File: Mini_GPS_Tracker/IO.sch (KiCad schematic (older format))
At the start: 10 parts, among them J1 Conn_ARM_JTAG_SWD_10, J4 Qwiic_Connector, SW1 SW_Push

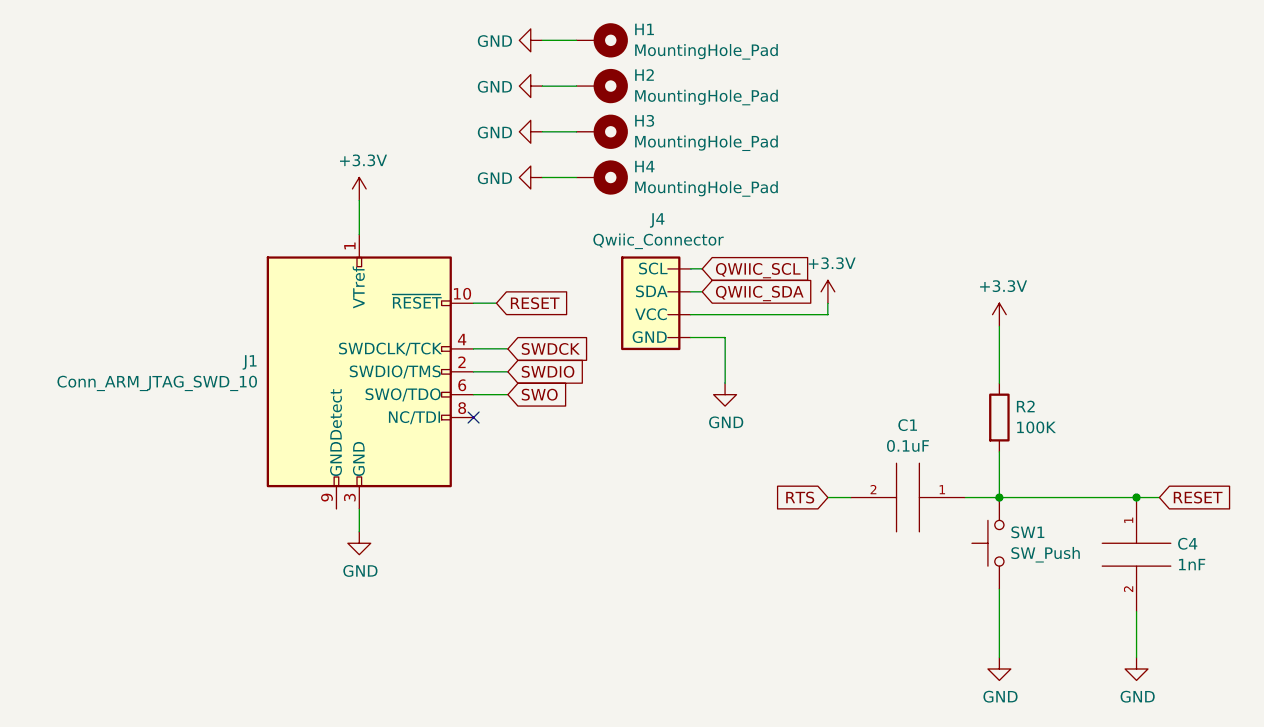
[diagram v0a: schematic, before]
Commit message: Add files via upload
Breaking out more pins
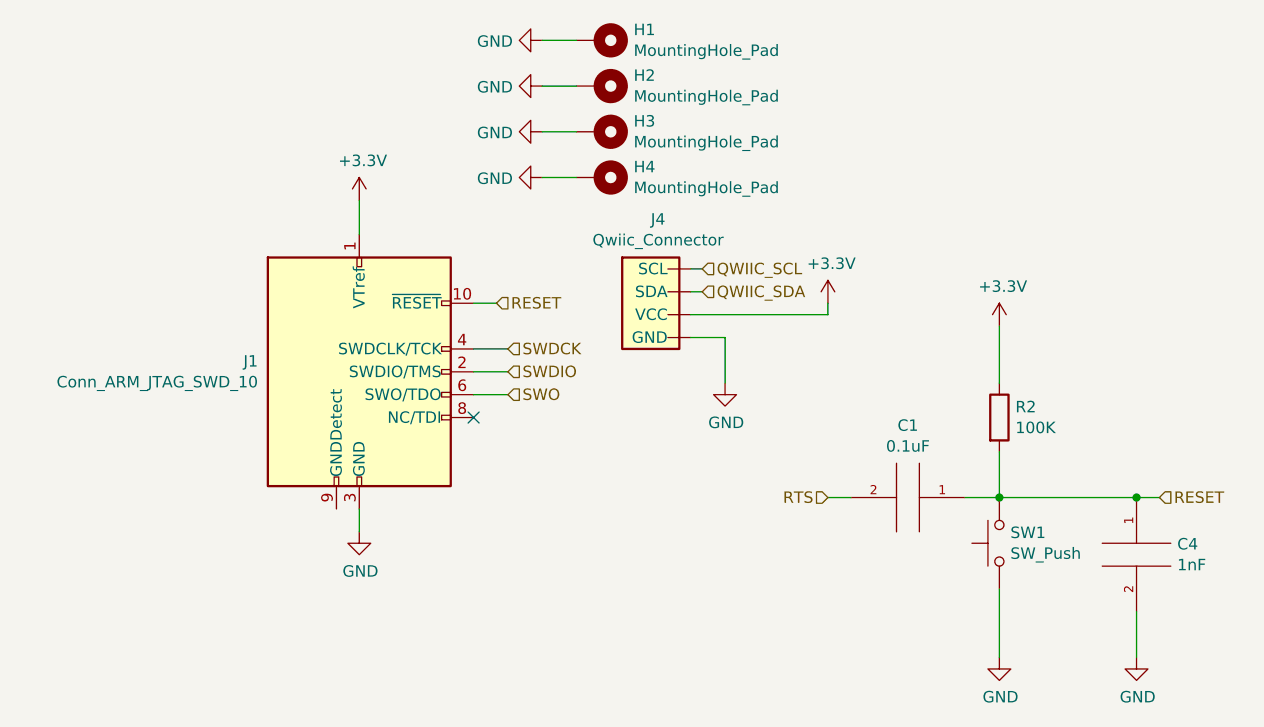
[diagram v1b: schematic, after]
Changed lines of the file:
@@
 Wire Wire Line
 	4700 3500 4800 3500
-Text GLabel 4850 3700 2    50   Input ~ 0
-SWDCK
-Text GLabel 4850 3800 2    50   Input ~ 0
-SWDIO
-Text GLabel 4800 3500 2    50   Input ~ 0
-RESET
-Text GLabel 4850 3900 2    50   Input ~ 0
-SWO
 $Comp
 L power:GND #PWR?
@@
 Wire Wire Line
 	5650 3550 6250 3550
-Text GLabel 5700 3350 2    50   Input ~ 0
-QWIIC_SCL
-Text GLabel 5700 3450 2    50   Input ~ 0
-QWIIC_SDA
 Wire Wire Line
 	5650 3350 5700 3350
 Wire Wire Line
 	5650 3450 5700 3450
-Text GLabel 6250 4350 0    50   Input ~ 0
-RTS
-Text GLabel 7700 4350 2    50   Input ~ 0
-RESET
 $Comp
 L pspice:CAP C?
@@
 Wire Wire Line
 	6250 3500 6250 3550
+Text HLabel 4800 3500 2    50   Input ~ 0
+RESET
+Text HLabel 4850 3700 2    50   Input ~ 0
+SWDCK
+Text HLabel 4850 3800 2    50   Input ~ 0
+SWDIO
+Text HLabel 4850 3900 2    50   Input ~ 0
+SWO
+Text HLabel 5700 3350 2    50   Input ~ 0
+QWIIC_SCL
+Text HLabel 5700 3450 2    50   Input ~ 0
+QWIIC_SDA
+Text HLabel 7700 4350 2    50   Input ~ 0
+RESET
+Text HLabel 6250 4350 0    50   Input ~ 0
+RTS
 $EndSCHEMATC
